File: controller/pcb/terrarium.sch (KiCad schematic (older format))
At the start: 57 parts, among them K1 G3MB-202P, K2 G3MB-202P, K3 G3MB-202P, Q1 S8050, Q2 S8050, Q3 S8050, SW1 RST, U1 ESP32-WROOM-32, U2 DS3231M, U5 TCA9548APWR

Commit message: pcb v1.7 done
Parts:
- added LED8: LED, Connector_JST:JST_XH_B3B-XH-A_1x03_P2.50mm_Vertical, symbol Connector_Generic:Conn_01x03
- added RESET_EEPROM: data, Connector_PinHeader_2.54mm:PinHeader_1x01_P2.54mm_Vertical, symbol Connector_Generic:Conn_01x01
- added U6: CAT24C256, Package_DIP:DIP-8_W7.62mm_Socket, symbol Memory_EEPROM:CAT24C256
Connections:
- net +3V3: now also U6.8 (VCC)
- net +5V: now also LED8.2 (Pin_2)
- net GND: now also LED8.1 (Pin_1), U6.1 (A0), U6.2 (A1), U6.3 (A2), U6.4 (GND)
- net SCL: now also U6.6 (SCL)
- net SDA: now also U6.5 (SDA)
- net at ALED1.2 (DOUT): now also LED8.3 (Pin_3)
- net G2: now reaches U1.23 (IO15)
- net G2: now also RESET_EEPROM.1 (Pin_1)
- no-connect marks 19 -> 17
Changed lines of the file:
@@
 Text Notes 3050 650  0    50   ~ 0
 Relays
-Wire Notes Line
-	700  5700 700  4350
 Text Notes 700  4300 0    50   ~ 0
 Status LED
@@
 	1350 5300 1350 5400
 Connection ~ 1350 5400
-NoConn ~ 1650 5000
 $Comp
 L Device:R_Small R5
@@
 NoConn ~ 10050 2200
 NoConn ~ 10050 2400
-NoConn ~ 10050 2500
 NoConn ~ 10050 3800
 NoConn ~ 10050 3900
@@
 	700  4350 2200 4350
 Wire Notes Line
-	2200 4350 2200 5700
-Wire Notes Line
-	2200 5700 700  5700
+	2200 6700 700  6700
 Wire Notes Line
 	6850 4700 6850 700
@@
 Text GLabel 10050 2300 2    50   Input ~ 0
 G13
+$Comp
+L Memory_EEPROM:CAT24C256 U6
+U 1 1 629D9AE3
+P 12200 5200
+F 0 "U6" H 12300 5450 50  0000 C CNN
+F 1 "CAT24C256" H 11900 5450 50  0000 C CNN
+F 2 "Package_DIP:DIP-8_W7.62mm_Socket" H 12200 5200 50  0001 C CNN
+F 3 "https://www.onsemi.cn/PowerSolutions/document/CAT24C256-D.PDF" H 12200 5200 50  0001 C CNN
+	1    12200 5200
+	1    0    0    -1
+$EndComp
+Text GLabel 12600 5100 2    50   Input ~ 0
+SDA
+Text GLabel 12600 5200 2    50   Input ~ 0
+SCL
+$Comp
+L power:GND #PWR0103
+U 1 1 629E21BF
+P 12200 5600
+F 0 "#PWR0103" H 12200 5350 50  0001 C CNN
+F 1 "GND" H 12205 5427 50  0000 C CNN
+F 2 "" H 12200 5600 50  0001 C CNN
+F 3 "" H 12200 5600 50  0001 C CNN
+	1    12200 5600
+	1    0    0    -1
+$EndComp
+Wire Wire Line
+	12200 5600 12200 5550
+Wire Wire Line
+	12200 5550 11800 5550
+Wire Wire Line
+	11800 5550 11800 5300
+Connection ~ 12200 5550
+Wire Wire Line
+	12200 5550 12200 5500
+Connection ~ 11800 5200
+Wire Wire Line
+	11800 5200 11800 5100
+Connection ~ 11800 5300
+Wire Wire Line
+	11800 5300 11800 5200
+$Comp
+L power:+3V3 #PWR0104
+U 1 1 629FC42C
+P 12200 4800
+F 0 "#PWR0104" H 12200 4650 50  0001 C CNN
+F 1 "+3V3" H 12215 4973 50  0000 C CNN
+F 2 "" H 12200 4800 50  0001 C CNN
+F 3 "" H 12200 4800 50  0001 C CNN
+	1    12200 4800
+	-1   0    0    -1
+$EndComp
+Wire Wire Line
+	12200 4800 12200 4900
+$Comp
+L Connector_Generic:Conn_01x03 LED8
+U 1 1 62B28163
+P 1400 6100
+F 0 "LED8" H 1480 6092 50  0000 L CNN
+F 1 "LED" H 1480 6001 50  0000 L CNN
+F 2 "Connector_JST:JST_XH_B3B-XH-A_1x03_P2.50mm_Vertical" H 1400 6100 50  0001 C CNN
+F 3 "~" H 1400 6100 50  0001 C CNN
+	1    1400 6100
+	-1   0    0    1
+$EndComp
+$Comp
+L power:GND #PWR020
+U 1 1 62B2816B
+P 1650 6250
+F 0 "#PWR020" H 1650 6000 50  0001 C CNN
+F 1 "GND" H 1655 6077 50  0000 C CNN
+F 2 "" H 1650 6250 50  0001 C CNN
+F 3 "" H 1650 6250 50  0001 C CNN
+	1    1650 6250
+	1    0    0    -1
+$EndComp
+Wire Wire Line
+	1650 6250 1650 6200
+Wire Wire Line
+	1650 6200 1600 6200
+$Comp
+L power:+5V #PWR021
+U 1 1 62B28173
+P 1900 6100
+F 0 "#PWR021" H 1900 5950 50  0001 C CNN
+F 1 "+5V" H 1915 6273 50  0000 C CNN
+F 2 "" H 1900 6100 50  0001 C CNN
+F 3 "" H 1900 6100 50  0001 C CNN
+	1    1900 6100
+	-1   0    0    -1
+$EndComp
+Wire Wire Line
+	1900 6100 1600 6100
+Wire Notes Line
+	2200 4350 2200 6700
+Wire Notes Line
+	700  4350 700  6700
+Wire Wire Line
+	1650 5000 1700 5000
+Wire Wire Line
+	1700 5000 1700 6000
+Wire Wire Line
+	1700 6000 1600 6000
+$Comp
+L Connector_Generic:Conn_01x01 RESET_EEPROM
+U 1 1 62BA3F8C
+P 7450 4000
+F 0 "RESET_EEPROM" H 7530 3992 50  0000 L CNN
+F 1 "data" H 7600 3400 50  0001 L CNN
+F 2 "Connector_PinHeader_2.54mm:PinHeader_1x01_P2.54mm_Vertical" H 7450 4000 50  0001 C CNN
+F 3 "~" H 7450 4000 50  0001 C CNN
+	1    7450 4000
+	0    -1   1    0
+$EndComp
+Text GLabel 7450 3800 1    50   Input ~ 0
+G2
+Text GLabel 10050 2500 2    50   Input ~ 0
+G2
 $EndSCHEMATC

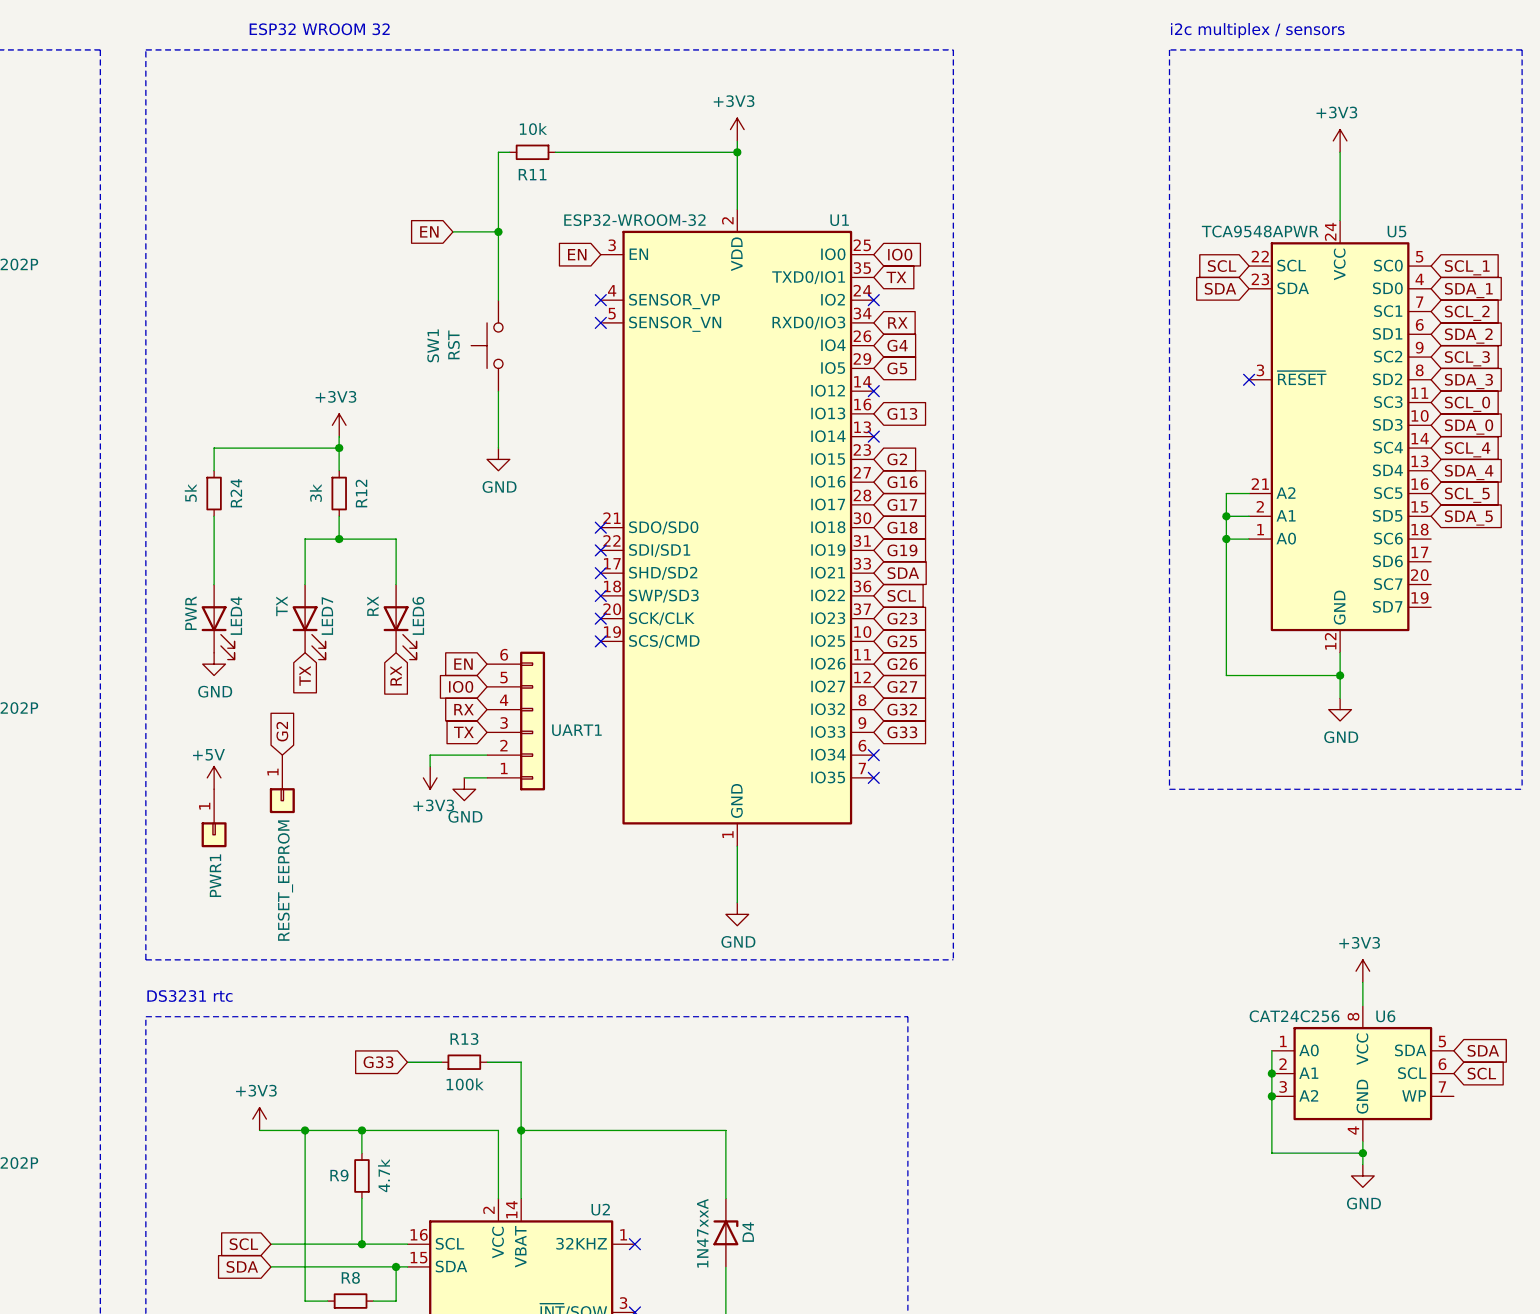
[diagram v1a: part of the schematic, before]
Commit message: change programming header to test pads
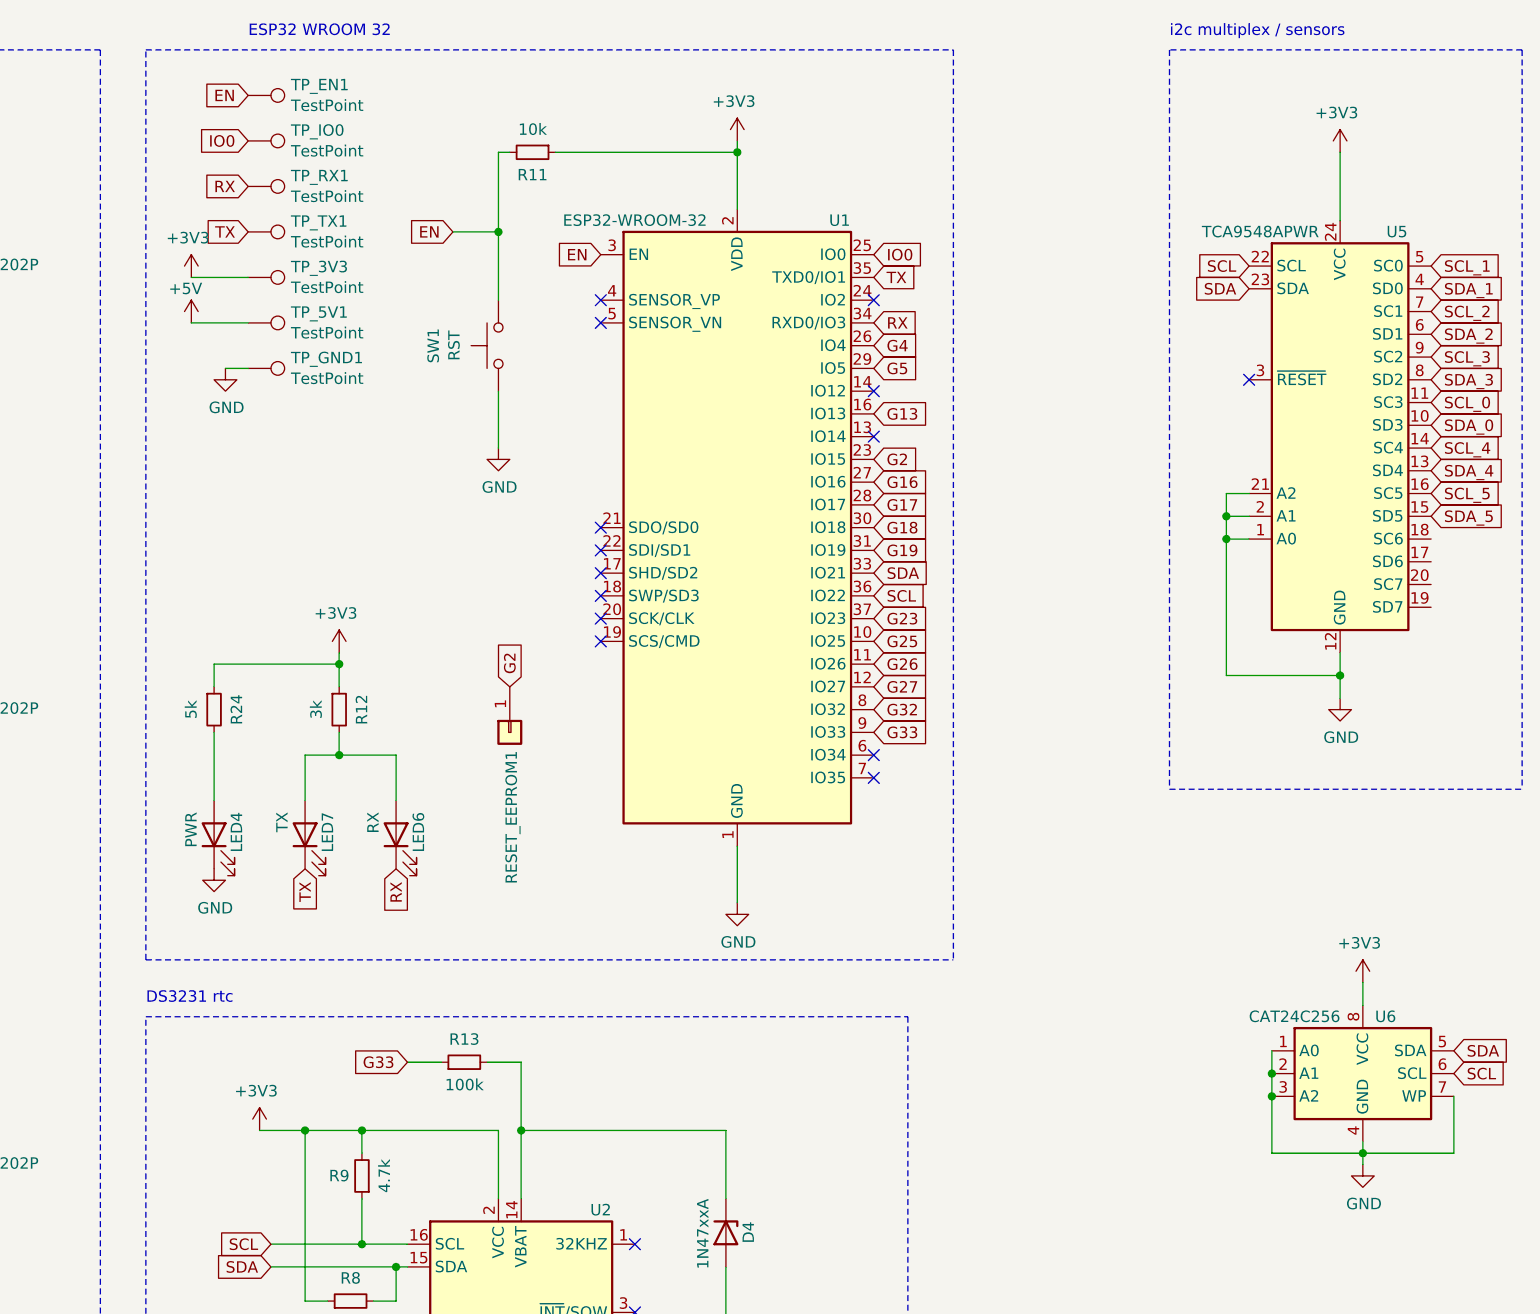
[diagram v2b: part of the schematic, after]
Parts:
- removed PWR1: data, Connector_PinHeader_2.54mm:PinHeader_1x01_P2.54mm_Vertical, symbol Connector_Generic:Conn_01x01
- removed UART1: data, Connector_PinHeader_2.54mm:PinHeader_1x06_P2.54mm_Vertical, symbol Connector_Generic:Conn_01x06
- added TP_3V3, TP_5V1, TP_EN1, TP_GND1, TP_IO0, TP_RX1, TP_TX1: TestPoint, TestPoint:TestPoint_Pad_1.5x1.5mm, symbol Connector:TestPoint
- renumbered RESET_EEPROM to RESET_EEPROM1
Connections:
- net +3V3: now also TP_3V3.1
- net +5V: now also TP_5V1.1
- net EN: now also TP_EN1.1
- net GND: now also U6.7 (WP), TP_GND1.1
- net IO0: now also TP_IO0.1
- net RX: now also TP_RX1.1
- net TX: now also TP_TX1.1
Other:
- moved on the sheet: LED4, LED6, LED7, R12, R24, RESET_EEPROM1
